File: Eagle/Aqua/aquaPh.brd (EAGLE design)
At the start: 100 x 80 mm, 19 parts, among them IC1 CA3140T, IC2 ICL7660CPA, IC3 TL072P

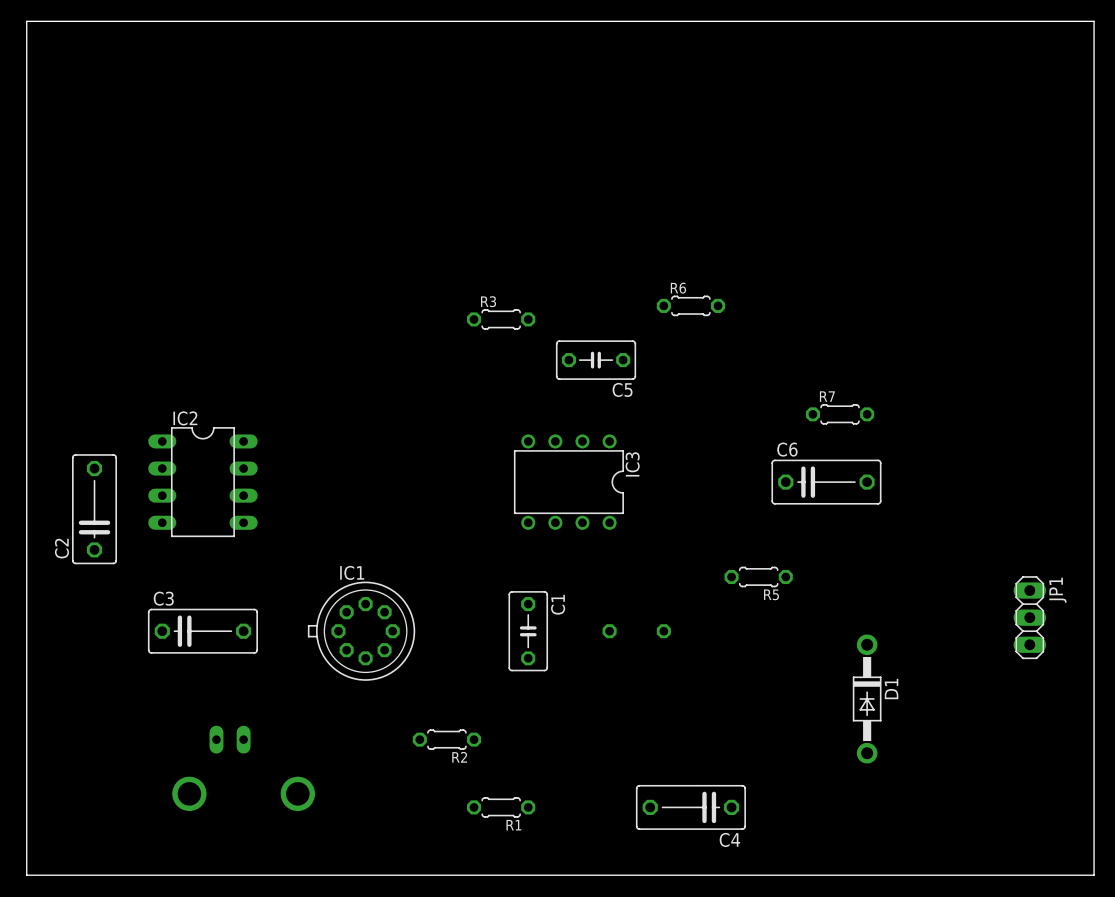
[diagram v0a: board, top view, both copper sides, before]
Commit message: Finished experimental board design Added PCB converted Arduino NANO <-> DIP 28
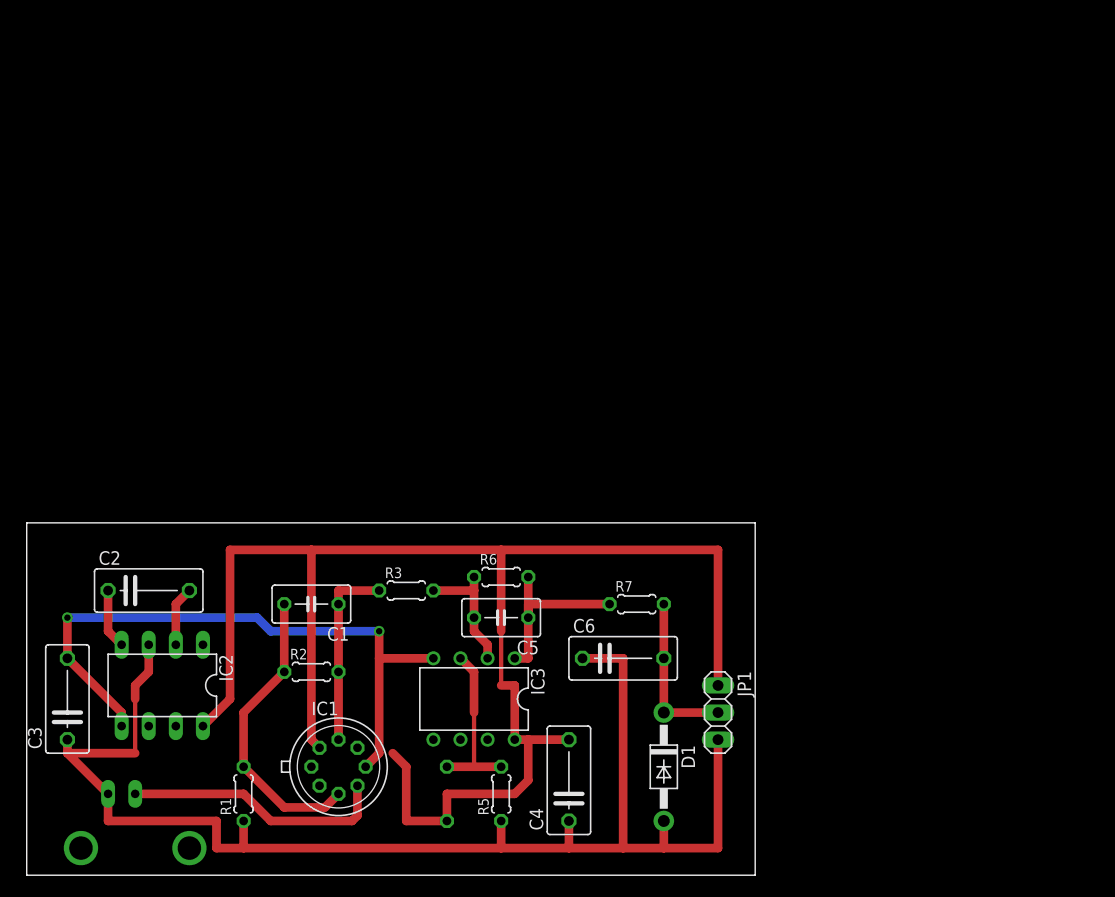
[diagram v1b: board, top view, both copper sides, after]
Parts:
- moved R5 31.5 mm to (44.5, 7.62), turned to 90 degrees
- moved R6 31.0 mm to (44.5, 27.9)
- moved JP1 30.5 mm to (64.8, 15.2)
- moved R3 26.9 mm to (35.6, 26.7)
- moved R7 26.1 mm to (57.1, 25.4)
- moved C5 25.7 mm to (44.5, 24.1)
- moved C6 25.2 mm to (55.9, 20.3)
- moved R1 24.2 mm to (20.3, 7.62), turned to 90 degrees
- moved R4 23.4 mm to (39.4, 7.62), turned to 270 degrees
- moved IC3 22.2 mm to (41.9, 16.5)
- moved C1 20.5 mm to (26.7, 25.4), turned to 180 degrees
- moved D1 20.1 mm to (59.7, 10.2)
- moved IC2 19.4 mm to (12.7, 17.8), turned to 180 degrees
- moved C3 14.2 mm to (3.81, 16.5), turned to 90 degrees
- moved R2 14.2 mm to (26.7, 19.1), turned to 0 degrees
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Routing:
- net +5V: track 0.00 -> 144.2 mm
- net GND: track 0.00 -> 127.8 mm
- net -5V: track 0.00 -> 60.3 mm, vias 0 -> 2
- net N$2: track 0.00 -> 27.8 mm
- net N$1: track 0.00 -> 24.9 mm
- net N$5: track 0.00 -> 17.8 mm
- net N$8: track 0.00 -> 17.8 mm
- net N$7: track 0.00 -> 15.8 mm
- net N$9: track 0.00 -> 15.2 mm
- net N$6: track 0.00 -> 12.0 mm
- net N$3: track 0.00 -> 5.61 mm
- net N$4: track 0.00 -> 5.61 mm
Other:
- board size 100 x 80 mm -> 68.2 x 33 mm

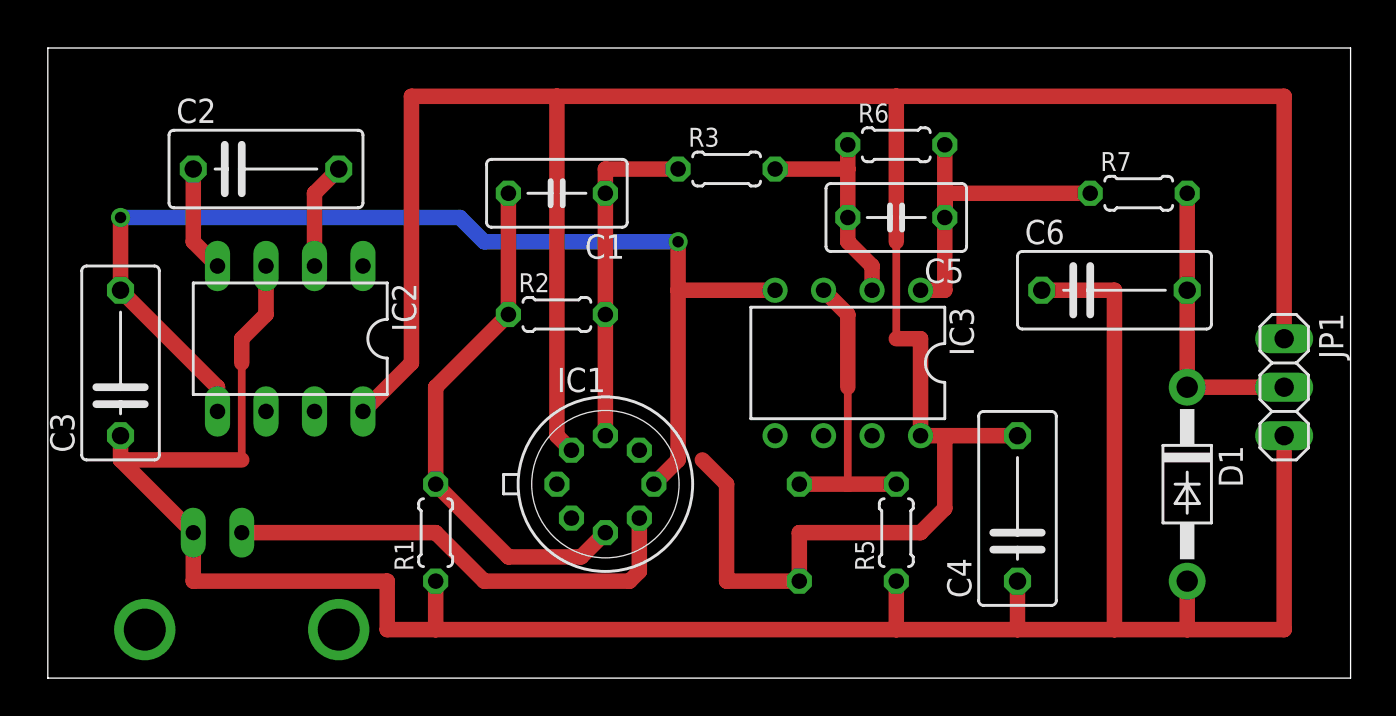
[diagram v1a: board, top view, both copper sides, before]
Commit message: Filled empty spaces with copper (faster eatching) Redone ArduinoNANO to DIP28 PCB to a single-side version Added V1 printout image
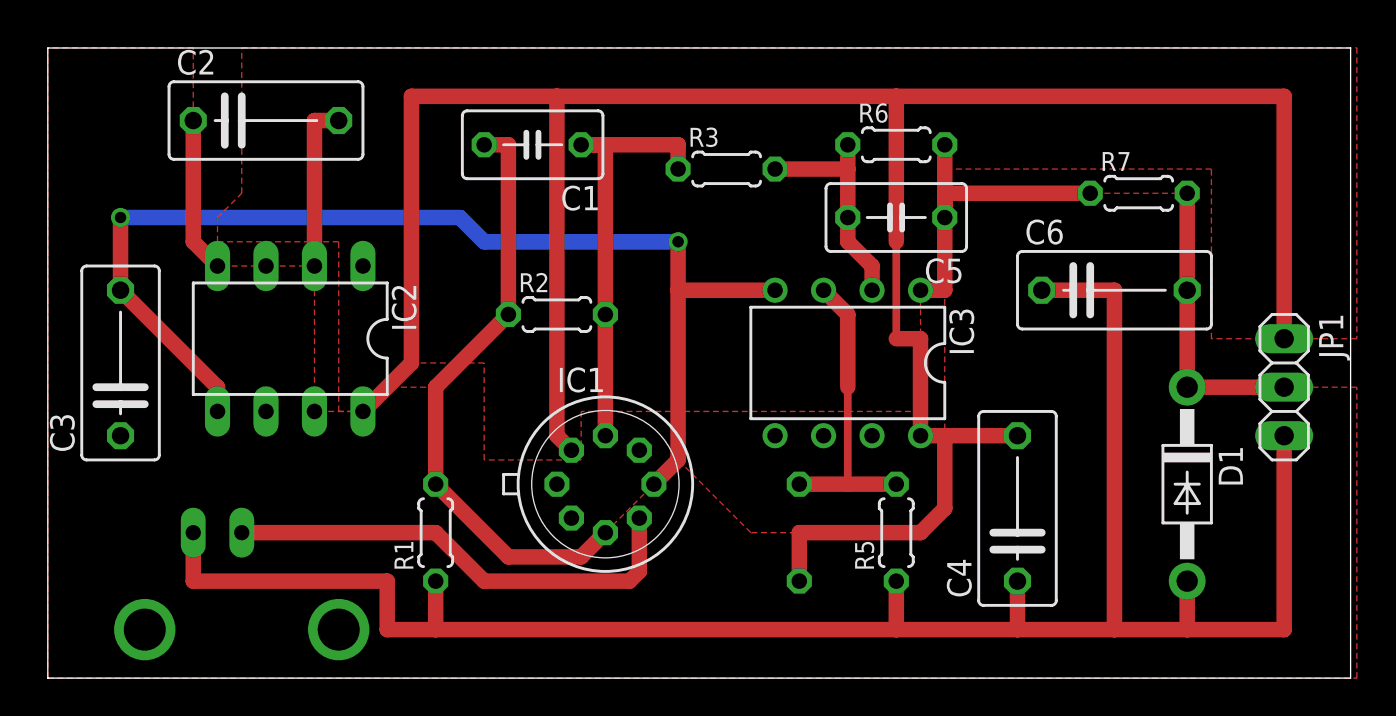
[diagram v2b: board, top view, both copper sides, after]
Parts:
- moved C1 2.84 mm to (25.4, 27.9)
- moved C2 2.54 mm to (11.4, 29.2)
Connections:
- net +5V renamed VCC
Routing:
- net GND: track 127.8 -> 104.1 mm
- net VCC: track 144.2 -> 133.5 mm
- net N$5: track 17.8 -> 22.9 mm
- net N$2: track 27.8 -> 31.6 mm
- net N$4: track 5.61 -> 8.89 mm
- net N$3: track 5.61 -> 8.15 mm
- added copper zone on layer 1, net GND
- added copper zone on layer 1, net VCC
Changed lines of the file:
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@@
 <element name="R3" library="rcl" package="0204/5" value="10k" x="35.56" y="26.67"/>
 <element name="R1" library="rcl" package="0204/5" value="33k" x="20.32" y="7.62" rot="R90"/>
-<element name="C1" library="rcl" package="C050-035X075" value="1uF" x="26.67" y="25.4" rot="R180"/>
-<element name="C2" library="rcl" package="C075-042X103" value="10uF" x="11.43" y="26.67"/>
+<element name="C1" library="rcl" package="C050-035X075" value="1uF" x="25.4" y="27.94" rot="R180"/>
+<element name="C2" library="rcl" package="C075-042X103" value="10uF" x="11.43" y="29.21"/>
 <element name="C3" library="rcl" package="C075-042X103" value="10uF" x="3.81" y="16.51" rot="R90"/>
 <element name="C4" library="rcl" package="C075-042X103" value="470uF" x="50.8" y="8.89" rot="R90"/>
@@
 <contactref element="R2" pad="1"/>
 <contactref element="C1" pad="2"/>
-<wire x1="24.13" y1="25.4" x2="24.13" y2="19.05" width="0.8128" layer="1"/>
+<wire x1="22.86" y1="27.94" x2="24.13" y2="27.94" width="0.8128" layer="1"/>
+<wire x1="24.13" y1="27.94" x2="24.13" y2="19.05" width="0.8128" layer="1"/>
 <wire x1="29.21" y1="7.62" x2="27.94" y2="6.35" width="0.8128" layer="1"/>
 <wire x1="27.94" y1="6.35" x2="24.13" y2="6.35" width="0.8128" layer="1"/>
@@
 <contactref element="C2" pad="1"/>
 <contactref element="IC2" pad="4"/>
-<wire x1="7.62" y1="26.67" x2="7.62" y2="22.86" width="0.8128" layer="1"/>
+<wire x1="7.62" y1="29.21" x2="7.62" y2="22.86" width="0.8128" layer="1"/>
 <wire x1="7.62" y1="22.86" x2="8.89" y2="21.59" width="0.8128" layer="1"/>
 </signal>
-<signal name="+5V">
+<signal name="VCC">
 <contactref element="IC1" pad="7"/>
 <contactref element="IC2" pad="8"/>
@@
 <wire x1="64.77" y1="17.78" x2="64.77" y2="30.48" width="0.8128" layer="1"/>
 <wire x1="64.77" y1="30.48" x2="44.45" y2="30.48" width="0.8128" layer="1"/>
-<wire x1="34.29" y1="11.43" x2="35.56" y2="10.16" width="0.8128" layer="1"/>
-<wire x1="35.56" y1="10.16" x2="35.56" y2="5.08" width="0.8128" layer="1"/>
-<wire x1="35.56" y1="5.08" x2="39.37" y2="5.08" width="0.8128" layer="1"/>
 <wire x1="39.37" y1="5.08" x2="39.37" y2="7.62" width="0.8128" layer="1"/>
 <wire x1="39.37" y1="7.62" x2="45.72" y2="7.62" width="0.8128" layer="1"/>
@@
 <wire x1="27.432" y1="11.938" x2="26.67" y2="12.7" width="0.8128" layer="1"/>
 <wire x1="26.67" y1="12.7" x2="26.67" y2="30.48" width="0.8128" layer="1"/>
+<polygon width="0.4064" layer="1" isolate="0.8128" orphans="yes">
+<vertex x="68.58" y="17.78"/>
+<vertex x="60.96" y="17.78"/>
+<vertex x="60.96" y="26.67"/>
+<vertex x="46.99" y="26.67"/>
+<vertex x="46.99" y="20.32"/>
+<vertex x="45.72" y="20.32"/>
+<vertex x="45.72" y="13.97"/>
+<vertex x="27.94" y="13.97"/>
+<vertex x="27.94" y="11.43"/>
+<vertex x="22.86" y="11.43"/>
+<vertex x="22.86" y="16.51"/>
+<vertex x="19.05" y="16.51"/>
+<vertex x="16.51" y="13.97"/>
+<vertex x="15.24" y="13.97"/>
+<vertex x="15.24" y="22.86"/>
+<vertex x="8.89" y="22.86"/>
+<vertex x="8.89" y="24.13"/>
+<vertex x="10.16" y="25.4"/>
+<vertex x="10.16" y="33.02"/>
+<vertex x="68.58" y="33.02"/>
+</polygon>
 </signal>
 <signal name="-5V">
@@
 <wire x1="17.78" y1="5.08" x2="17.78" y2="2.54" width="0.8128" layer="1"/>
 <wire x1="20.32" y1="5.08" x2="20.32" y2="2.54" width="0.8128" layer="1"/>
-<wire x1="3.81" y1="11.43" x2="7.62" y2="7.62" width="0.8128" layer="1"/>
-<wire x1="11.43" y1="21.59" x2="11.43" y2="19.05" width="0.8128" layer="1"/>
-<wire x1="11.43" y1="19.05" x2="10.16" y2="17.78" width="0.8128" layer="1"/>
-<wire x1="10.16" y1="17.78" x2="10.16" y2="16.51" width="0.8128" layer="1"/>
-<wire x1="3.81" y1="12.7" x2="3.81" y2="11.43" width="0.8128" layer="1"/>
-<wire x1="3.81" y1="11.43" x2="10.16" y2="11.43" width="0.8128" layer="1"/>
-<wire x1="10.16" y1="16.51" x2="10.16" y2="11.43" width="0.4064" layer="1"/>
 <wire x1="64.77" y1="12.7" x2="64.77" y2="2.54" width="0.8128" layer="1"/>
 <wire x1="64.77" y1="2.54" x2="59.69" y2="2.54" width="0.8128" layer="1"/>
+<polygon width="0.4064" layer="1" isolate="0.8128" orphans="yes">
+<vertex x="68.58" y="15.24"/>
+<vertex x="59.69" y="15.24"/>
+<vertex x="59.69" y="25.4"/>
+<vertex x="46.99" y="25.4"/>
+<vertex x="46.99" y="8.89"/>
+<vertex x="45.72" y="7.62"/>
+<vertex x="36.83" y="7.62"/>
+<vertex x="33.02" y="11.43"/>
+<vertex x="27.94" y="6.35"/>
+<vertex x="24.13" y="6.35"/>
+<vertex x="20.32" y="10.16"/>
+<vertex x="20.32" y="15.24"/>
+<vertex x="17.78" y="15.24"/>
+<vertex x="16.51" y="13.97"/>
+<vertex x="13.97" y="13.97"/>
+<vertex x="13.97" y="21.59"/>
+<vertex x="8.89" y="21.59"/>
+<vertex x="7.62" y="22.86"/>
+<vertex x="7.62" y="33.02"/>
+<vertex x="0" y="33.02"/>
+<vertex x="0" y="0"/>
+<vertex x="68.58" y="0"/>
+</polygon>
 </signal>
 <signal name="N$4">
 <contactref element="C2" pad="2"/>
 <contactref element="IC2" pad="2"/>
-<wire x1="15.24" y1="26.67" x2="13.97" y2="25.4" width="0.8128" layer="1"/>
-<wire x1="13.97" y1="25.4" x2="13.97" y2="21.59" width="0.8128" layer="1"/>
+<wire x1="15.24" y1="29.21" x2="13.97" y2="29.21" width="0.8128" layer="1"/>
+<wire x1="13.97" y1="29.21" x2="13.97" y2="21.59" width="0.8128" layer="1"/>
 </signal>
 <signal name="N$5">
@@
 <contactref element="C1" pad="1"/>
 <contactref element="R3" pad="1"/>
-<wire x1="33.02" y1="26.67" x2="29.21" y2="26.67" width="0.8128" layer="1"/>
-<wire x1="29.21" y1="26.67" x2="29.21" y2="25.4" width="0.8128" layer="1"/>
-<wire x1="29.21" y1="25.4" x2="29.21" y2="19.05" width="0.8128" layer="1"/>
+<wire x1="33.02" y1="26.67" x2="33.02" y2="27.94" width="0.8128" layer="1"/>
+<wire x1="33.02" y1="27.94" x2="27.94" y2="27.94" width="0.8128" layer="1"/>
+<wire x1="27.94" y1="27.94" x2="29.21" y2="27.94" width="0.8128" layer="1"/>
+<wire x1="29.21" y1="27.94" x2="29.21" y2="19.05" width="0.8128" layer="1"/>
 <wire x1="29.21" y1="19.05" x2="29.21" y2="12.7" width="0.8128" layer="1"/>
 </signal>
@@
 </signal>
 </signals>
-<errors>
-</errors>
 </board>
 </drawing>

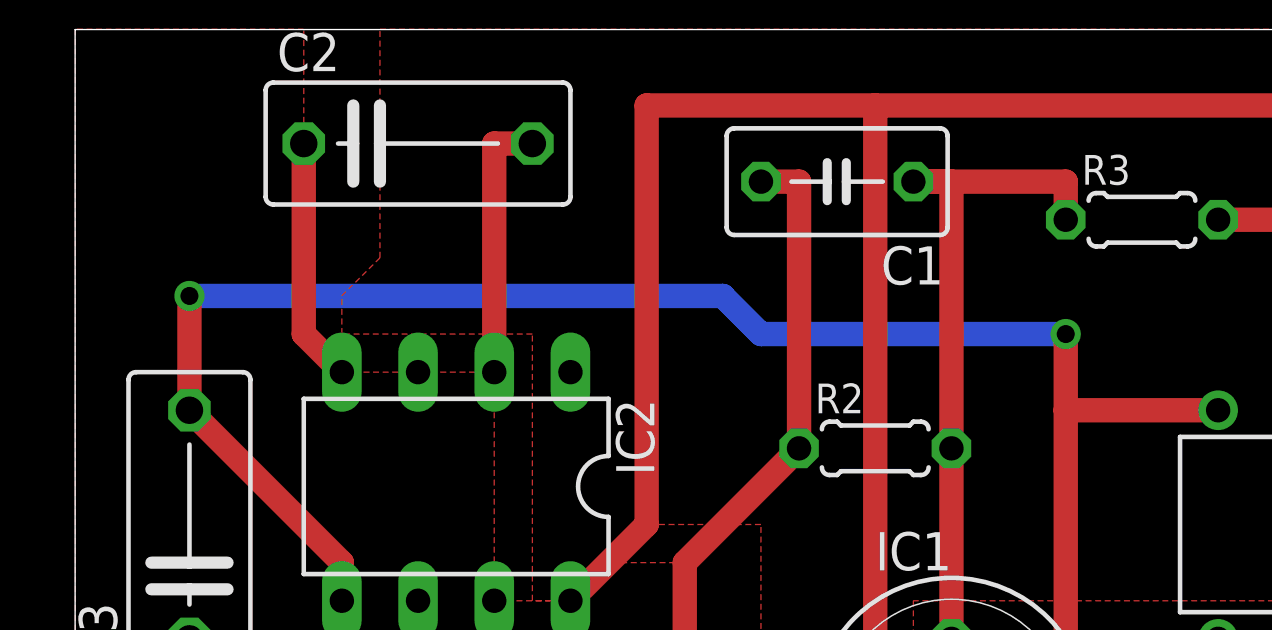
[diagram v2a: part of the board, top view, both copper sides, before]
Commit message: Big update Many important fixes dictated by 1st prototype
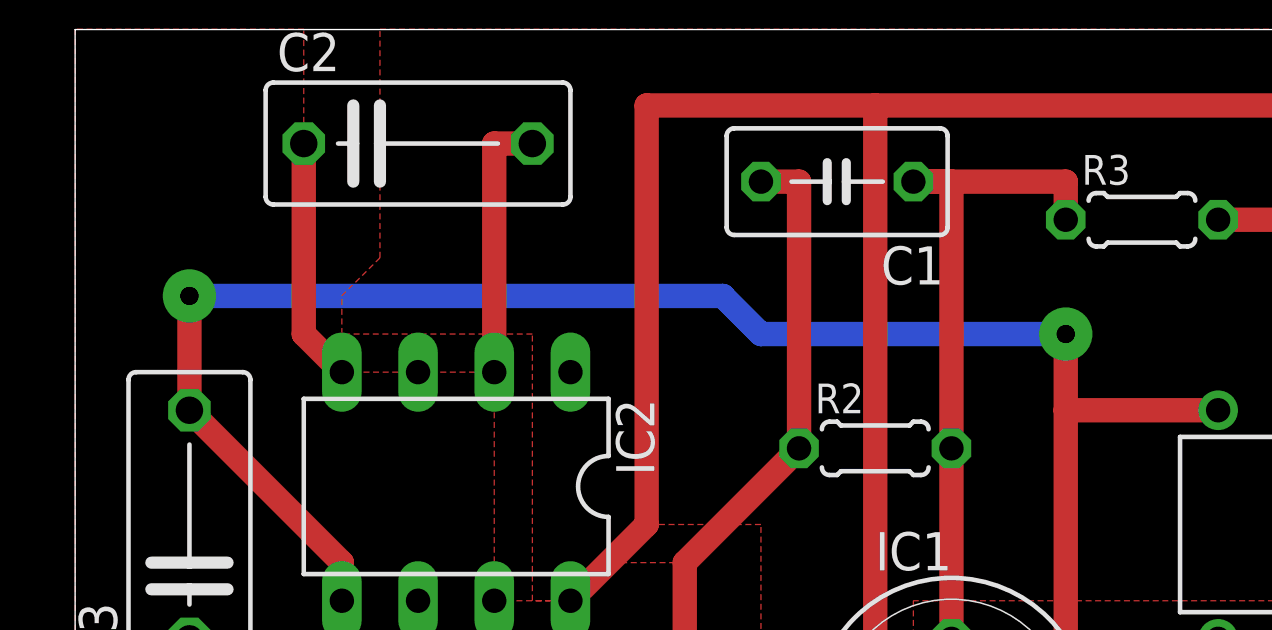
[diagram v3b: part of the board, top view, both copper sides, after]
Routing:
- net -5V: vias 2 -> 4
